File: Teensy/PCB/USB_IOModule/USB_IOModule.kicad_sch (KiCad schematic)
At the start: 23 parts, among them J1 USB_B, J2 USB_A, J3 Power_Connector_2x3, U1 SC16IS762IPW, U2 Teensy4.0, X1 XO53

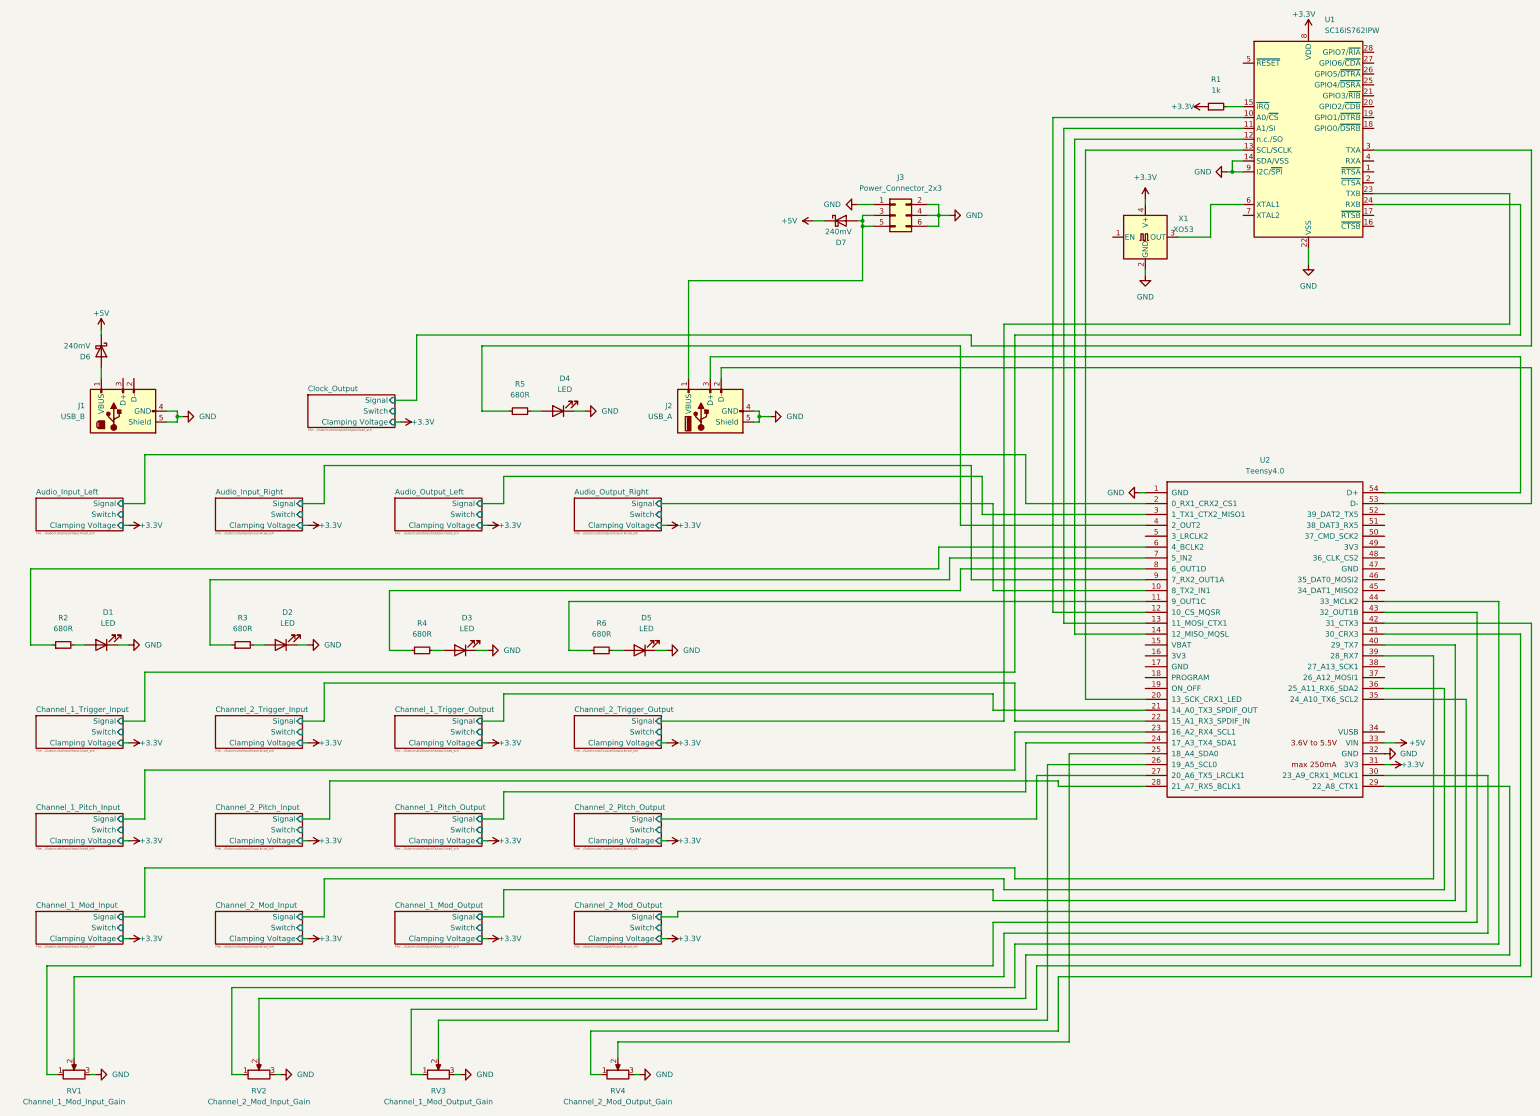
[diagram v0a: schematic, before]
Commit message: Replaced Schematic Lines with references
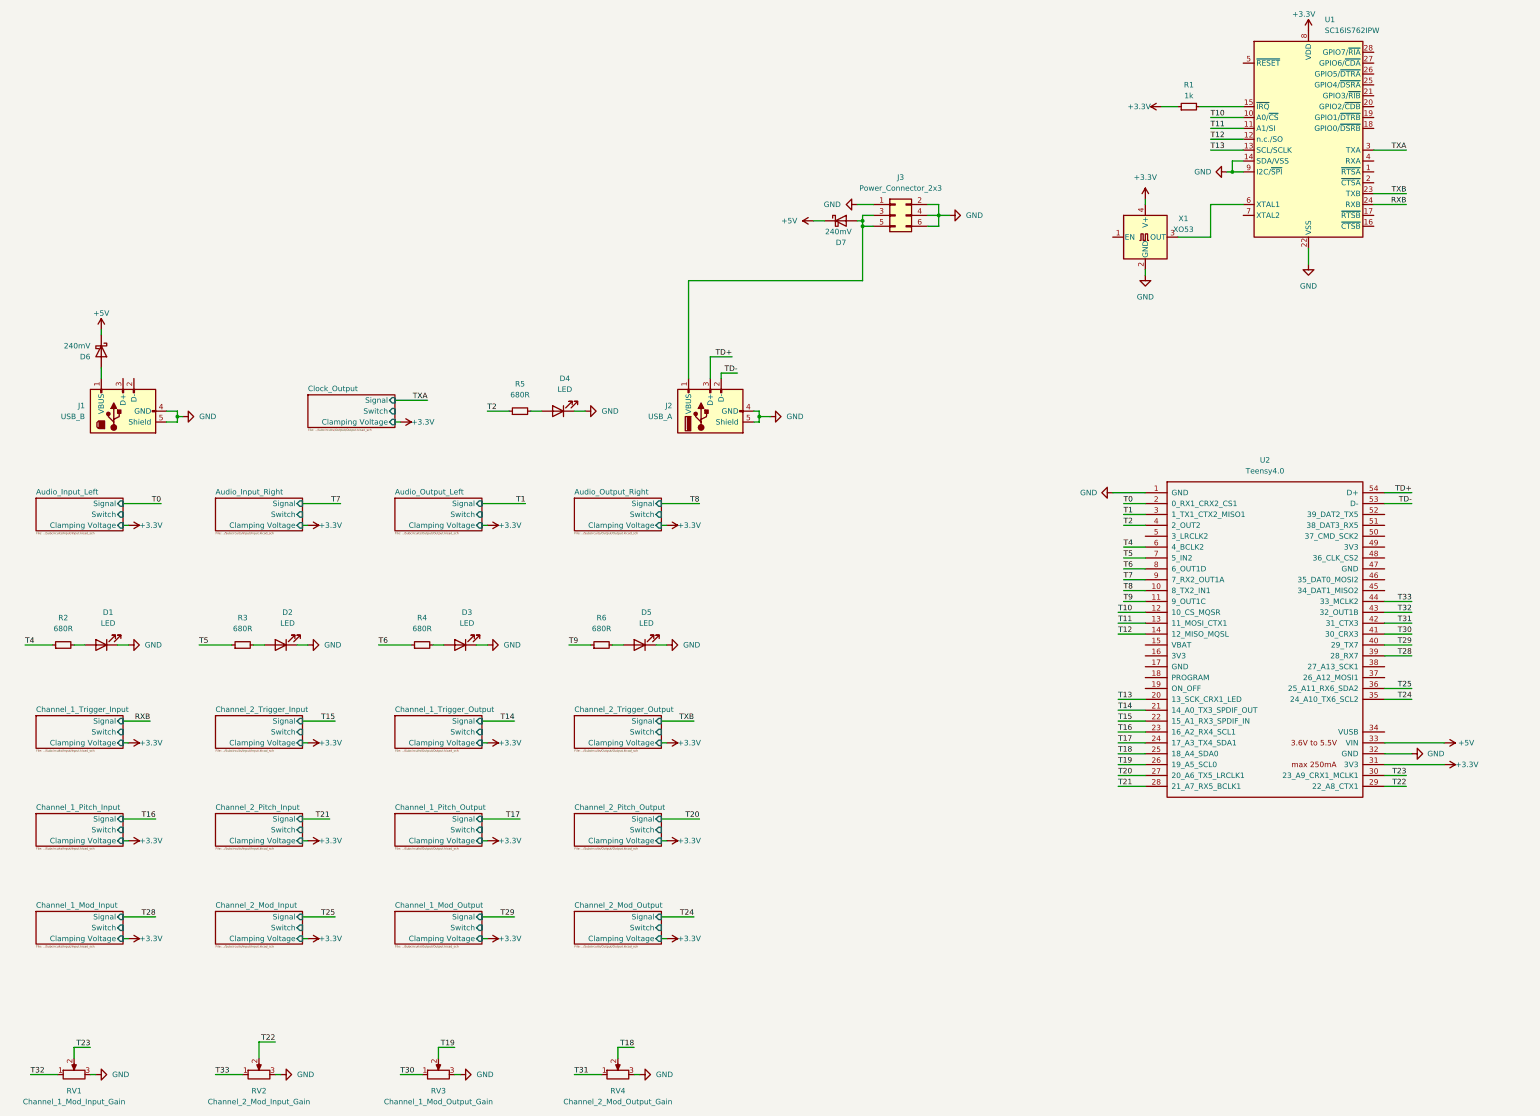
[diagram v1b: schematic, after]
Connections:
- net T30: now reaches RV3.1, U2.41 (30_CRX3)
- net T19: now reaches RV3.2, U2.26 (19_A5_SCL0)
- net T4: now reaches R2.1, U2.6 (4_BCLK2)
- net T9: now reaches R6.1, U2.11 (9_OUT1C)
- net T2: now reaches R5.1, U2.4 (2_OUT2)
- net T10: now reaches U1.10 (A0/~{CS}), U2.12 (10_CS_MQSR)
- net T11: now reaches U1.11 (A1/SI), U2.13 (11_MOSI_CTX1)
- net T12: now reaches U1.12 (n.c./SO), U2.14 (12_MISO_MQSL)
- net T13: now reaches U1.13 (SCL/SCLK), U2.20 (13_SCK_CRX1_LED)
- net T6: now reaches R4.1, U2.8 (6_OUT1D)
- net T33: now reaches RV2.1, U2.44 (33_MCLK2)
- net T22: now reaches RV2.2, U2.29 (22_A8_CTX1)
- net T5: now reaches R3.1, U2.7 (5_IN2)
- net T32: now reaches RV1.1, U2.43 (32_OUT1B)
- net T23: now reaches RV1.2, U2.30 (23_A9_CRX1_MCLK1)
- net T18: now reaches RV4.2, U2.25 (18_A4_SDA0)
- net T31: now reaches RV4.1, U2.42 (31_CTX3)
- net TD-: now reaches J2.2 (D-), U2.53 (D-)
- net TD+: now reaches J2.3 (D+), U2.54 (D+)
- net Audio_Input_Left/Signal renamed T0
- net Audio_Input_Right/Signal renamed T7
- net Audio_Output_Left/Signal renamed T1
- net Audio_Output_Right/Signal renamed T8
- net Channel_1_Mod_Input/Signal renamed T28
- net Channel_1_Mod_Output/Signal renamed T29
- net Channel_1_Pitch_Input/Signal renamed T16
- net Channel_1_Pitch_Output/Signal renamed T17
- net Channel_1_Trigger_Input/Signal renamed RXB
- net Channel_1_Trigger_Output/Signal renamed T14
- net Channel_2_Mod_Input/Signal renamed T25
- net Channel_2_Mod_Output/Signal renamed T24
- net Channel_2_Pitch_Input/Signal renamed T21
- net Channel_2_Pitch_Output/Signal renamed T20
- net Channel_2_Trigger_Input/Signal renamed T15
- net Channel_2_Trigger_Output/Signal renamed TXB
- net Clock_Output/Signal renamed TXA
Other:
- moved on the sheet: D3, D5, R1, R4, R6
